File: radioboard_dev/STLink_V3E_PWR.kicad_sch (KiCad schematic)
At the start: 65 parts

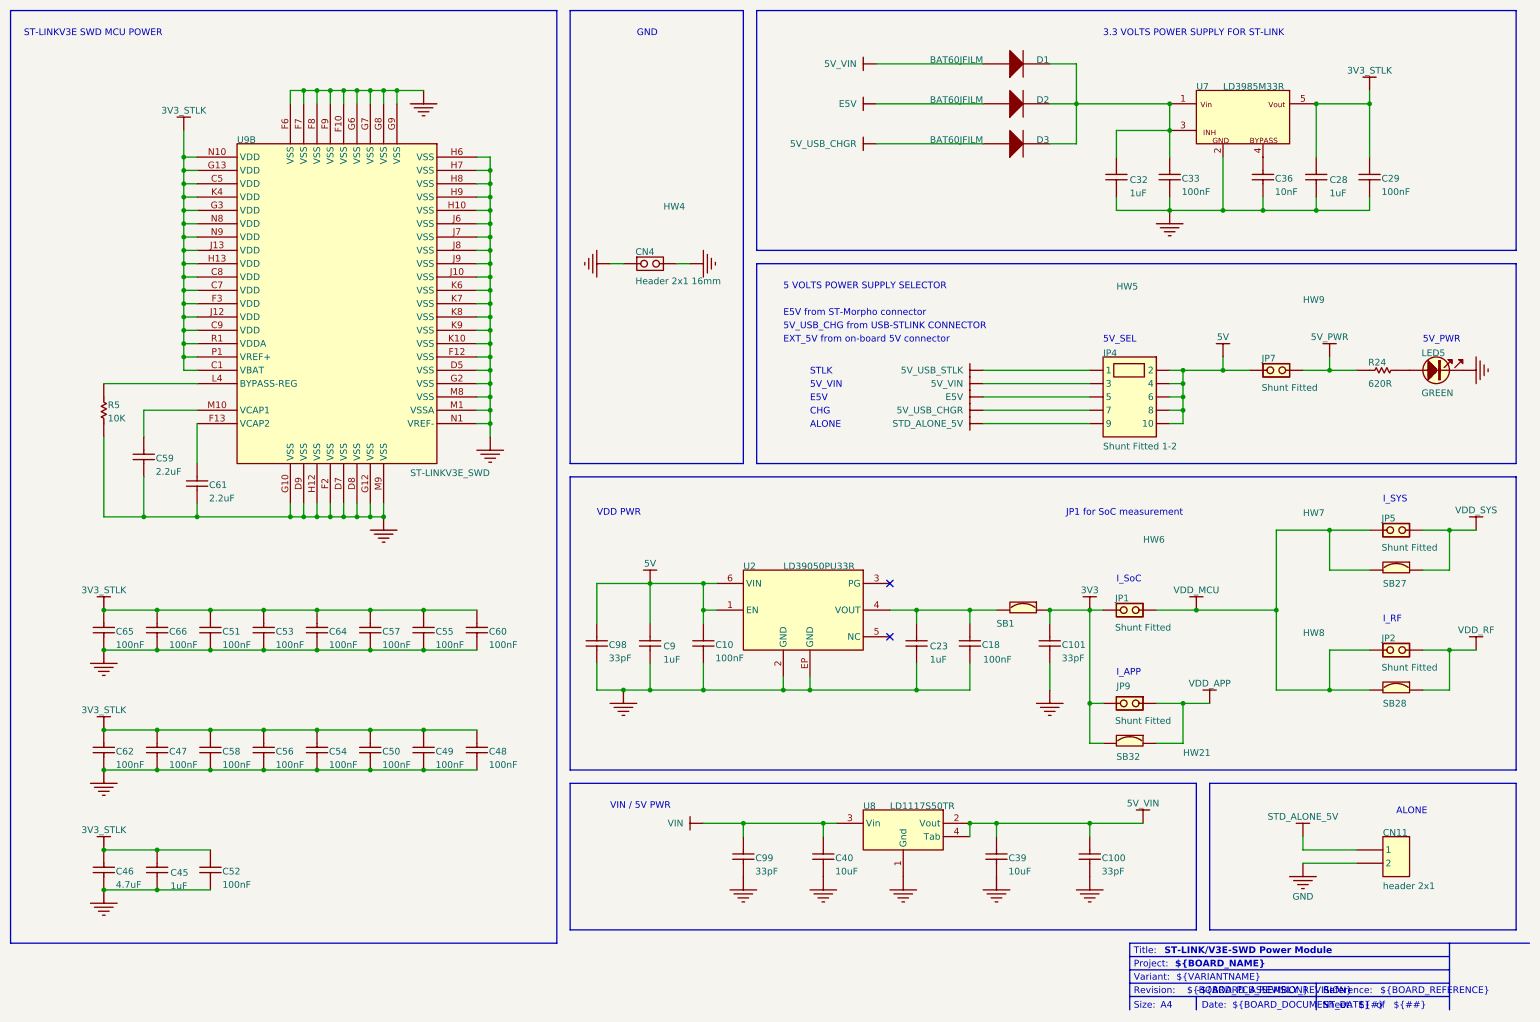
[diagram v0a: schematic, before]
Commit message: added components
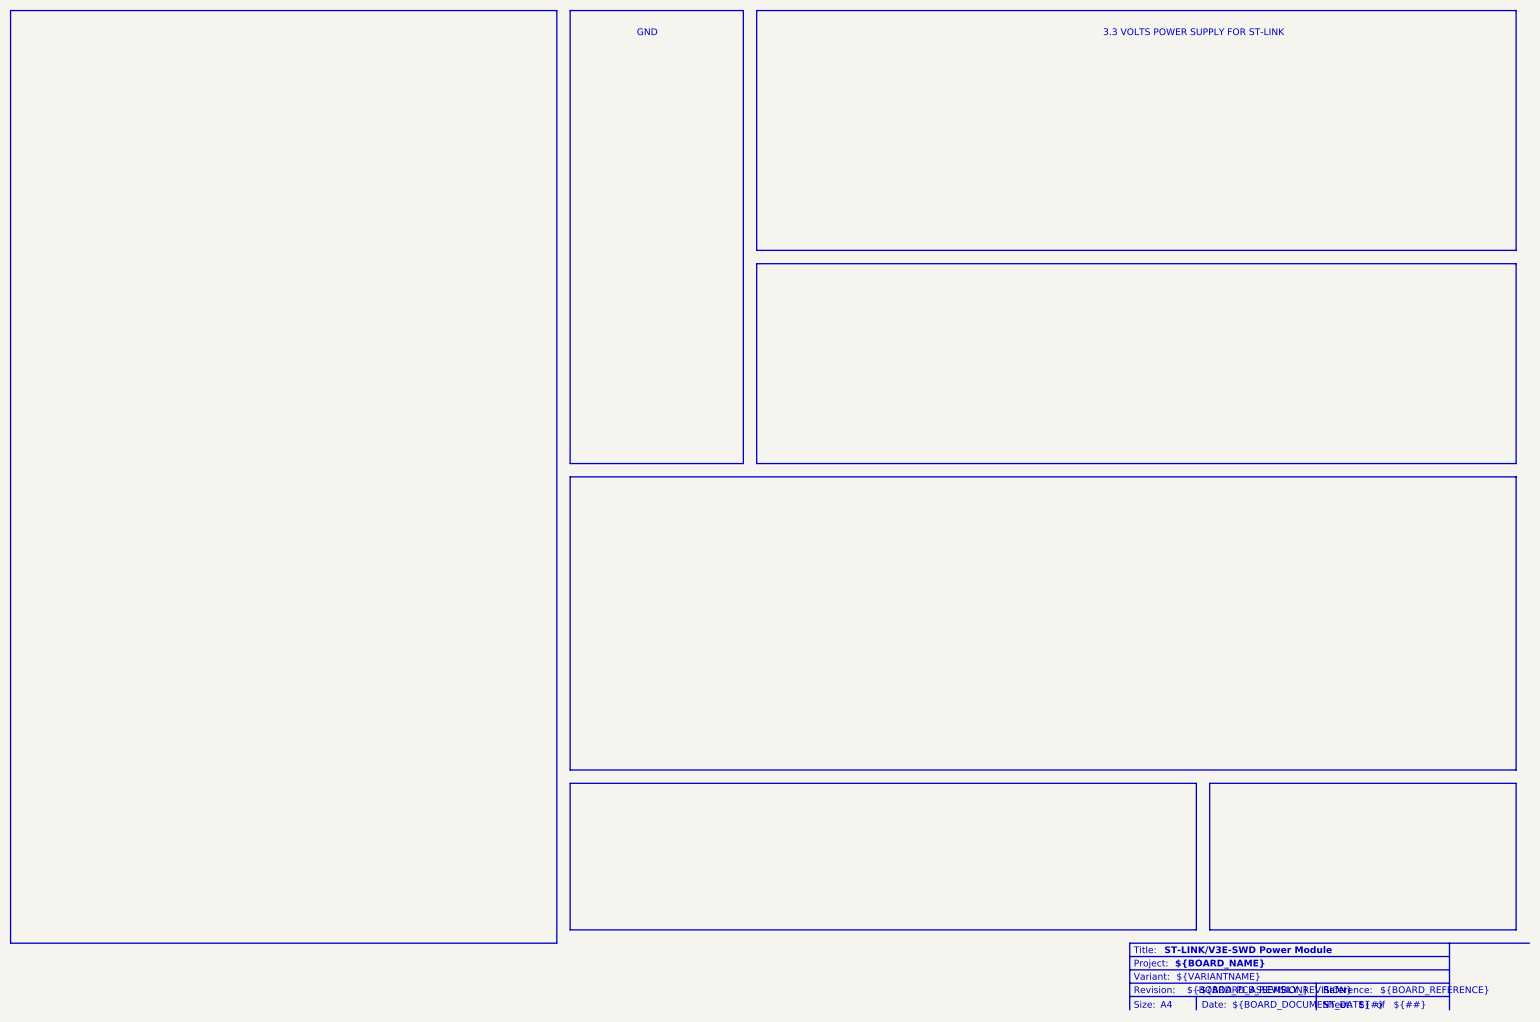
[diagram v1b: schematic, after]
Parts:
- removed C10, C100, C101, C18, C29, C33, C36, C47, C48, C49, C50, C51, C52, C53, C54, C55, C56, C57, C58, C60, C62, C64, C65, C66, C98, C99: (no value), C0402, symbol MB1389-altium-import:U_STLink_V3E_PWR_1_Capacitor
- removed C23, C28, C32, C45, C46, C59, C61, C9: (no value), C0603, symbol MB1389-altium-import:U_STLink_V3E_PWR_1_Capacitor
- removed C39, C40: (no value), C0805, symbol MB1389-altium-import:U_STLink_V3E_PWR_1_Capacitor
- removed CN11: (no value), CON_988-JIUBABA_PHFS25-11-02-G0B115-T-1, symbol MB1389-altium-import:U_STLink_V3E_PWR_0_Header 2x1
- removed CN4: (no value), CON_SAMTEC_TSW-102-09-X-S, symbol MB1389-altium-import:U_STLink_V3E_PWR_0_Jumper_Header 2x1
- removed D1, D2, D3: (no value), DIO_SOD323, symbol MB1389-altium-import:U_STLink_V3E_PWR_2_BAT60JFILM
- removed HW21, HW4, HW5, HW6, HW7, HW8, HW9: (no value), symbol MB1389-altium-import:U_STLink_V3E_PWR_0_Shunt Black 2.54mm
- removed JP1, JP2, JP5, JP7, JP9: (no value), CON_SAMTEC_TSW-102-07-G-S, symbol MB1389-altium-import:U_STLink_V3E_PWR_0_Jumper_Header 2x1 Fitted
- removed JP4: (no value), CON_SAMTEC_TSW-105-07-X-D, symbol MB1389-altium-import:U_STLink_V3E_PWR_0_Jumper_Header 5x2 Fitted 1-2
- removed LED5: (no value), LED_0603_OSRAM_LG-Q396-PS-35_GREEN_1A2K_H0P4, symbol MB1389-altium-import:U_STLink_V3E_PWR_0_LED_green_0
- removed R24: (no value), R0402, symbol MB1389-altium-import:U_STLink_V3E_PWR_0_Resistor
- removed R5: (no value), R0402, symbol MB1389-altium-import:U_STLink_V3E_PWR_1_Resistor
- removed SB1, SB27, SB28, SB32: (no value), SOLDER-BRIDGE_R0603-0R, symbol MB1389-altium-import:U_STLink_V3E_PWR_0_SB_ON
- removed U2: (no value), ICC_DFN6-EPAD_3X3_P095, symbol MB1389-altium-import:U_STLink_V3E_PWR_0_LD39050PU33R
- removed U7: (no value), REG_SOT23-5L, symbol MB1389-altium-import:U_STLink_V3E_PWR_0_LD3985M33R
- removed U8: (no value), REG_SOT223-TAB, symbol MB1389-altium-import:U_STLink_V3E_PWR_0_LD1117S50TR
- removed U9: (no value), ICC_UFBGA201_176+25_10X10_P065, symbol MB1389-altium-import:U_STLink_V3E_PWR_0_ST-LINKV3E_SWD
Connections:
- no-connect marks 2 -> 0
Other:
- note removed: "5 VOLTS POWER SUPPLY SELECTOR"
- note removed: "5V_PWR"
- note removed: "5V_SEL"
- note removed: "5V_USB_CHG from USB-STLINK CONNECTOR"
- note removed: "5V_VIN"
- note removed: "ALONE"
- note removed: "CHG"
- note removed: "E5V"
- note removed: "E5V from ST-Morpho connector"
- note removed: "EXT_5V from on-board 5V connector"
- note removed: "I_APP"
- note removed: "I_RF"
- note removed: "I_SYS"
- note removed: "I_SoC"
- note removed: "JP1 for SoC measurement"
- note removed: "ST-LINKV3E SWD MCU POWER"
- note removed: "STLK"
- note removed: "VDD PWR"
- note removed: "VIN / 5V PWR"
